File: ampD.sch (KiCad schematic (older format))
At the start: 9 parts, among them U3 MCP6004, U4 Mux

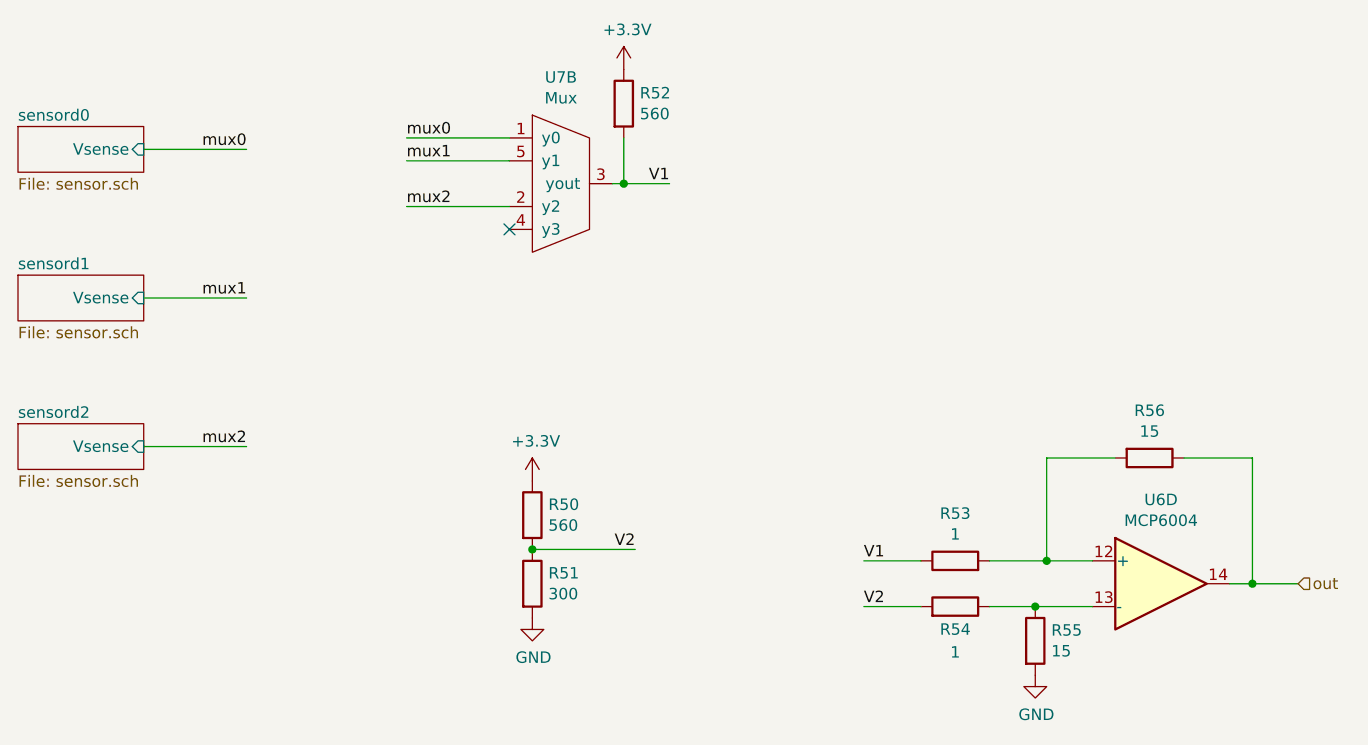
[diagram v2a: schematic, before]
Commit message: fixed drc errors
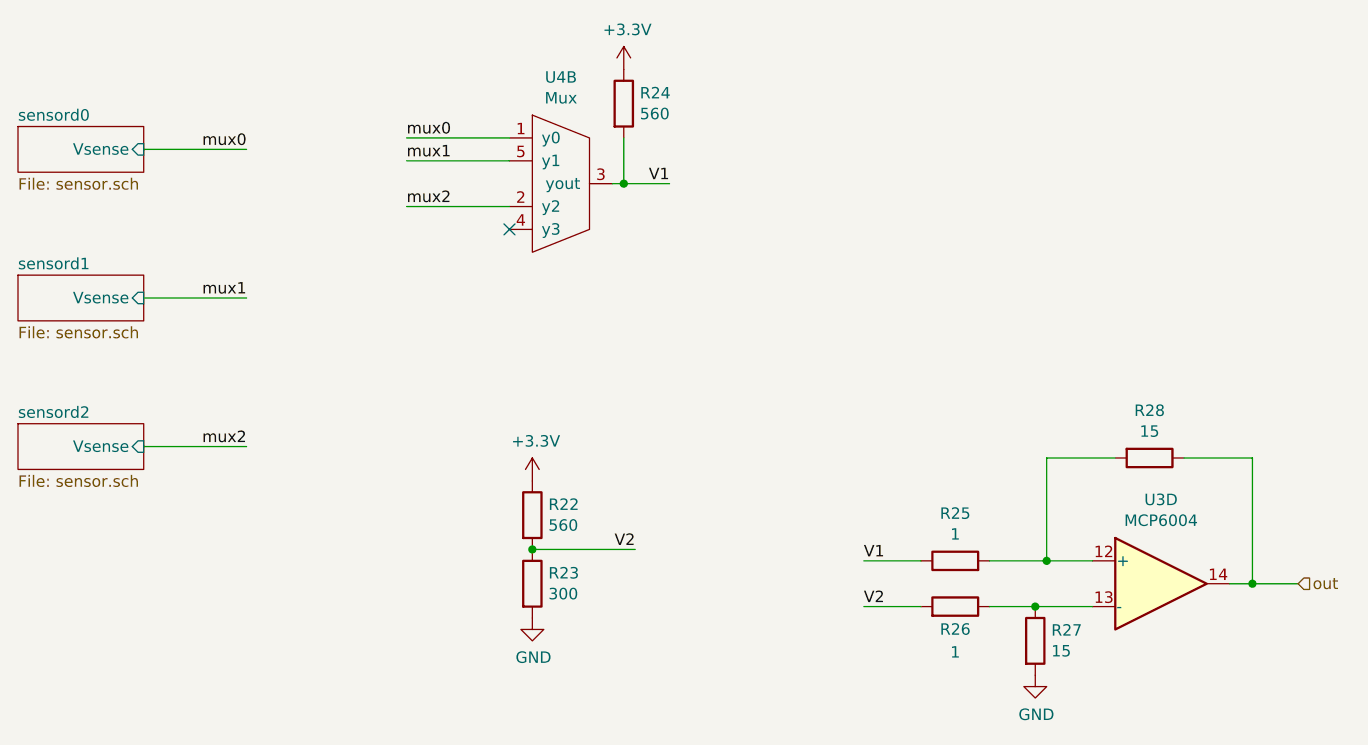
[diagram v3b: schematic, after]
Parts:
- U3: footprint Package_DIP:DIP-14_W7.62mm -> Package_SO:SOIC-16_3.9x9.9mm_P1.27mm
- U4: footprint Package_DIP:DIP-16_W7.62mm -> Package_SO:SOIC-16_3.9x9.9mm_P1.27mm
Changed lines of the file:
@@
 AR Path="/6019DBCE/6015EF5C" Ref="R27"  Part="1"
 AR Path="/601B4C19/6015EF5C" Ref="R55"  Part="1"
-F 0 "R55" H 5520 4096 50  0000 L CNN
+F 0 "R27" H 5520 4096 50  0000 L CNN
 F 1 "15" H 5520 4005 50  0000 L CNN
 F 2 "Resistor_THT:R_Axial_DIN0204_L3.6mm_D1.6mm_P5.08mm_Horizontal" V 5380 4050 50  0001 C CNN
@@
 AR Path="/6019DBCE/6019E3A7" Ref="R28"  Part="1"
 AR Path="/601B4C19/6019E3A7" Ref="R56"  Part="1"
-F 0 "R56" V 5743 3250 50  0000 C CNN
+F 0 "R28" V 5743 3250 50  0000 C CNN
 F 1 "15" V 5834 3250 50  0000 C CNN
 F 2 "Resistor_THT:R_Axial_DIN0204_L3.6mm_D1.6mm_P5.08mm_Horizontal" V 5880 3250 50  0001 C CNN
@@
 AR Path="/6019DBCE/6019E3B2" Ref="R25"  Part="1"
 AR Path="/601B4C19/6019E3B2" Ref="R53"  Part="1"
-F 0 "R53" V 5307 3700 50  0000 C CNN
+F 0 "R25" V 5307 3700 50  0000 C CNN
 F 1 "1" V 5216 3700 50  0000 C CNN
 F 2 "Resistor_THT:R_Axial_DIN0204_L3.6mm_D1.6mm_P5.08mm_Horizontal" V 5030 3700 50  0001 C CNN
@@
 AR Path="/6019DBCE/6019E3A8" Ref="R26"  Part="1"
 AR Path="/601B4C19/6019E3A8" Ref="R54"  Part="1"
-F 0 "R54" V 5000 3900 50  0000 C CNN
+F 0 "R26" V 5000 3900 50  0000 C CNN
 F 1 "1" V 4900 3900 50  0000 C CNN
 F 2 "Resistor_THT:R_Axial_DIN0204_L3.6mm_D1.6mm_P5.08mm_Horizontal" V 5030 3900 50  0001 C CNN
@@
 AR Path="/6019DBCE/6019E3B3" Ref="R22"  Part="1"
 AR Path="/601B4C19/6019E3B3" Ref="R50"  Part="1"
-F 0 "R50" H 3320 3546 50  0000 L CNN
+F 0 "R22" H 3320 3546 50  0000 L CNN
 F 1 "560" H 3320 3455 50  0000 L CNN
 F 2 "Resistor_THT:R_Axial_DIN0204_L3.6mm_D1.6mm_P5.08mm_Horizontal" V 3180 3500 50  0001 C CNN
@@
 AR Path="/6019DBCE/60198F36" Ref="R23"  Part="1"
 AR Path="/601B4C19/60198F36" Ref="R51"  Part="1"
-F 0 "R51" H 3320 3846 50  0000 L CNN
+F 0 "R23" H 3320 3846 50  0000 L CNN
 F 1 "300" H 3320 3755 50  0000 L CNN
 F 2 "Resistor_THT:R_Axial_DIN0204_L3.6mm_D1.6mm_P5.08mm_Horizontal" V 3180 3800 50  0001 C CNN
@@
 AR Path="/6019DBCE/6017A5CD" Ref="U4"  Part="2"
 AR Path="/601B4C19/6017A5CD" Ref="U7"  Part="2"
-F 0 "U7" H 3375 2515 50  0000 C CNN
+F 0 "U4" H 3375 2515 50  0000 C CNN
 F 1 "Mux" H 3375 2424 50  0000 C CNN
-F 2 "Package_DIP:DIP-16_W7.62mm" H 3350 2050 50  0001 C CNN
+F 2 "Package_SO:SOIC-16_3.9x9.9mm_P1.27mm" H 3350 2050 50  0001 C CNN
 F 3 "" H 3350 2050 50  0001 C CNN
 	2    3350 2050
@@
 AR Path="/6019DBCE/6018F24E" Ref="U3"  Part="4"
 AR Path="/601B4C19/6018F24E" Ref="U6"  Part="4"
-F 0 "U6" H 6000 4167 50  0000 C CNN
+F 0 "U3" H 6000 4167 50  0000 C CNN
 F 1 "MCP6004" H 6000 4076 50  0000 C CNN
-F 2 "Package_DIP:DIP-14_W7.62mm" H 5950 3900 50  0001 C CNN
+F 2 "Package_SO:SOIC-16_3.9x9.9mm_P1.27mm" H 5950 3900 50  0001 C CNN
 F 3 "http://ww1.microchip.com/downloads/en/DeviceDoc/21733j.pdf" H 6050 4000 50  0001 C CNN
 	4    6000 3800
@@
 AR Path="/6019DBCE/60204E98" Ref="R24"  Part="1"
 AR Path="/601B4C19/60204E98" Ref="R52"  Part="1"
-F 0 "R52" H 3720 1746 50  0000 L CNN
+F 0 "R24" H 3720 1746 50  0000 L CNN
 F 1 "560" H 3720 1655 50  0000 L CNN
 F 2 "Resistor_THT:R_Axial_DIN0204_L3.6mm_D1.6mm_P5.08mm_Horizontal" V 3580 1700 50  0001 C CNN

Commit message: switched over remaining rs to 0805
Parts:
- R22, R23, R24, R25, R26, R27, R28: footprint Resistor_THT:R_Axial_DIN0204_L3.6mm_D1.6mm_P5.08mm_Horizontal -> Resistor_SMD:R_0805_2012Metric_Pad1.20x1.40mm_HandSolder
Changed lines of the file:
@@
 F 0 "R27" H 5520 4096 50  0000 L CNN
 F 1 "15" H 5520 4005 50  0000 L CNN
-F 2 "Resistor_THT:R_Axial_DIN0204_L3.6mm_D1.6mm_P5.08mm_Horizontal" V 5380 4050 50  0001 C CNN
+F 2 "Resistor_SMD:R_0805_2012Metric_Pad1.20x1.40mm_HandSolder" V 5380 4050 50  0001 C CNN
 F 3 "~" H 5450 4050 50  0001 C CNN
 	1    5450 4050
@@
 F 0 "R28" V 5743 3250 50  0000 C CNN
 F 1 "15" V 5834 3250 50  0000 C CNN
-F 2 "Resistor_THT:R_Axial_DIN0204_L3.6mm_D1.6mm_P5.08mm_Horizontal" V 5880 3250 50  0001 C CNN
+F 2 "Resistor_SMD:R_0805_2012Metric_Pad1.20x1.40mm_HandSolder" V 5880 3250 50  0001 C CNN
 F 3 "~" H 5950 3250 50  0001 C CNN
 	1    5950 3250
@@
 F 0 "R25" V 5307 3700 50  0000 C CNN
 F 1 "1" V 5216 3700 50  0000 C CNN
-F 2 "Resistor_THT:R_Axial_DIN0204_L3.6mm_D1.6mm_P5.08mm_Horizontal" V 5030 3700 50  0001 C CNN
+F 2 "Resistor_SMD:R_0805_2012Metric_Pad1.20x1.40mm_HandSolder" V 5030 3700 50  0001 C CNN
 F 3 "~" H 5100 3700 50  0001 C CNN
 	1    5100 3700
@@
 F 0 "R26" V 5000 3900 50  0000 C CNN
 F 1 "1" V 4900 3900 50  0000 C CNN
-F 2 "Resistor_THT:R_Axial_DIN0204_L3.6mm_D1.6mm_P5.08mm_Horizontal" V 5030 3900 50  0001 C CNN
+F 2 "Resistor_SMD:R_0805_2012Metric_Pad1.20x1.40mm_HandSolder" V 5030 3900 50  0001 C CNN
 F 3 "~" H 5100 3900 50  0001 C CNN
 	1    5100 3900
@@
 F 0 "R22" H 3320 3546 50  0000 L CNN
 F 1 "560" H 3320 3455 50  0000 L CNN
-F 2 "Resistor_THT:R_Axial_DIN0204_L3.6mm_D1.6mm_P5.08mm_Horizontal" V 3180 3500 50  0001 C CNN
+F 2 "Resistor_SMD:R_0805_2012Metric_Pad1.20x1.40mm_HandSolder" V 3180 3500 50  0001 C CNN
 F 3 "~" H 3250 3500 50  0001 C CNN
 	1    3250 3500
@@
 F 0 "R23" H 3320 3846 50  0000 L CNN
 F 1 "300" H 3320 3755 50  0000 L CNN
-F 2 "Resistor_THT:R_Axial_DIN0204_L3.6mm_D1.6mm_P5.08mm_Horizontal" V 3180 3800 50  0001 C CNN
+F 2 "Resistor_SMD:R_0805_2012Metric_Pad1.20x1.40mm_HandSolder" V 3180 3800 50  0001 C CNN
 F 3 "~" H 3250 3800 50  0001 C CNN
 	1    3250 3800
@@
 F 0 "R24" H 3720 1746 50  0000 L CNN
 F 1 "560" H 3720 1655 50  0000 L CNN
-F 2 "Resistor_THT:R_Axial_DIN0204_L3.6mm_D1.6mm_P5.08mm_Horizontal" V 3580 1700 50  0001 C CNN
+F 2 "Resistor_SMD:R_0805_2012Metric_Pad1.20x1.40mm_HandSolder" V 3580 1700 50  0001 C CNN
 F 3 "~" H 3650 1700 50  0001 C CNN
 	1    3650 1700

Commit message: fixed issue with wrong amp footprint
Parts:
- U3: footprint Package_SO:SOIC-16_3.9x9.9mm_P1.27mm -> Package_SO:SOIC-14_3.9x8.7mm_P1.27mm
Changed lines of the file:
@@
 F 0 "U3" H 6000 4167 50  0000 C CNN
 F 1 "MCP6004" H 6000 4076 50  0000 C CNN
-F 2 "Package_SO:SOIC-16_3.9x9.9mm_P1.27mm" H 5950 3900 50  0001 C CNN
+F 2 "Package_SO:SOIC-14_3.9x8.7mm_P1.27mm" H 5950 3900 50  0001 C CNN
 F 3 "http://ww1.microchip.com/downloads/en/DeviceDoc/21733j.pdf" H 6050 4000 50  0001 C CNN
 	4    6000 3800

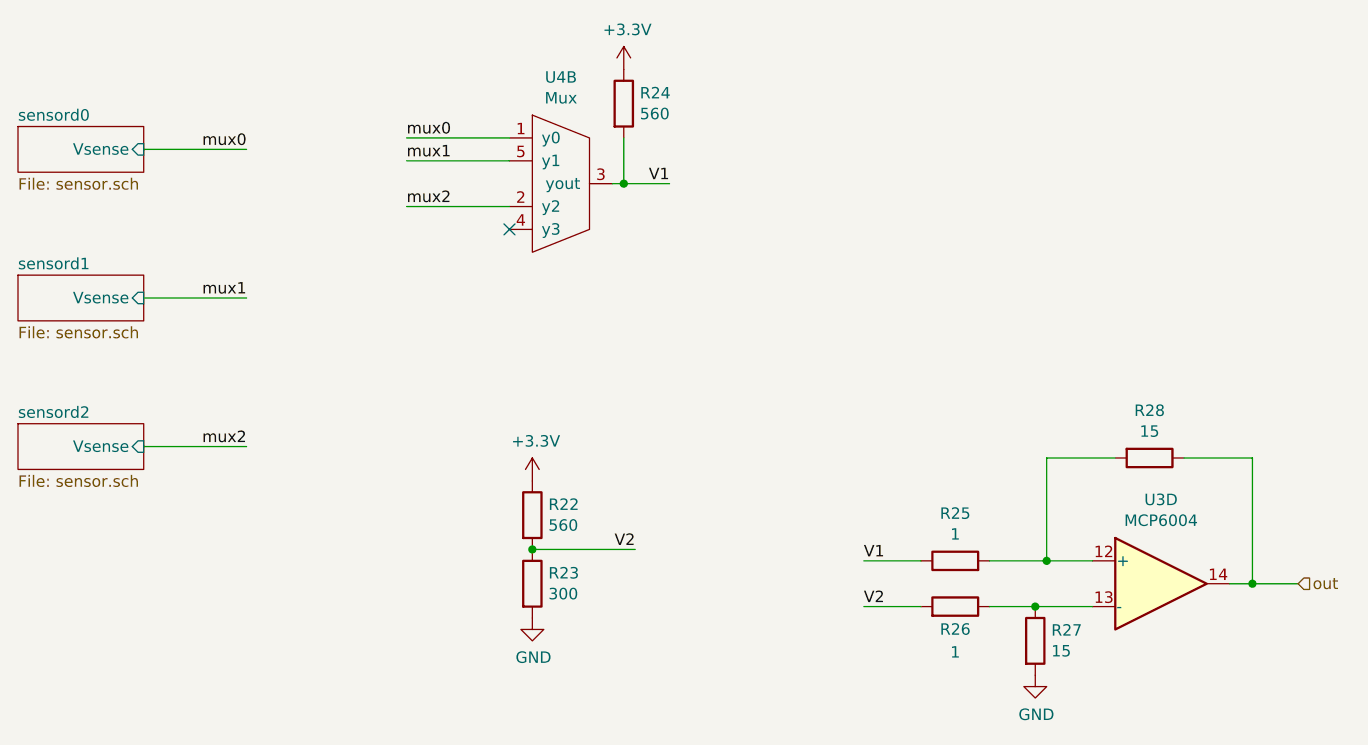
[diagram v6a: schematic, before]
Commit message: reverted back to screw terminals
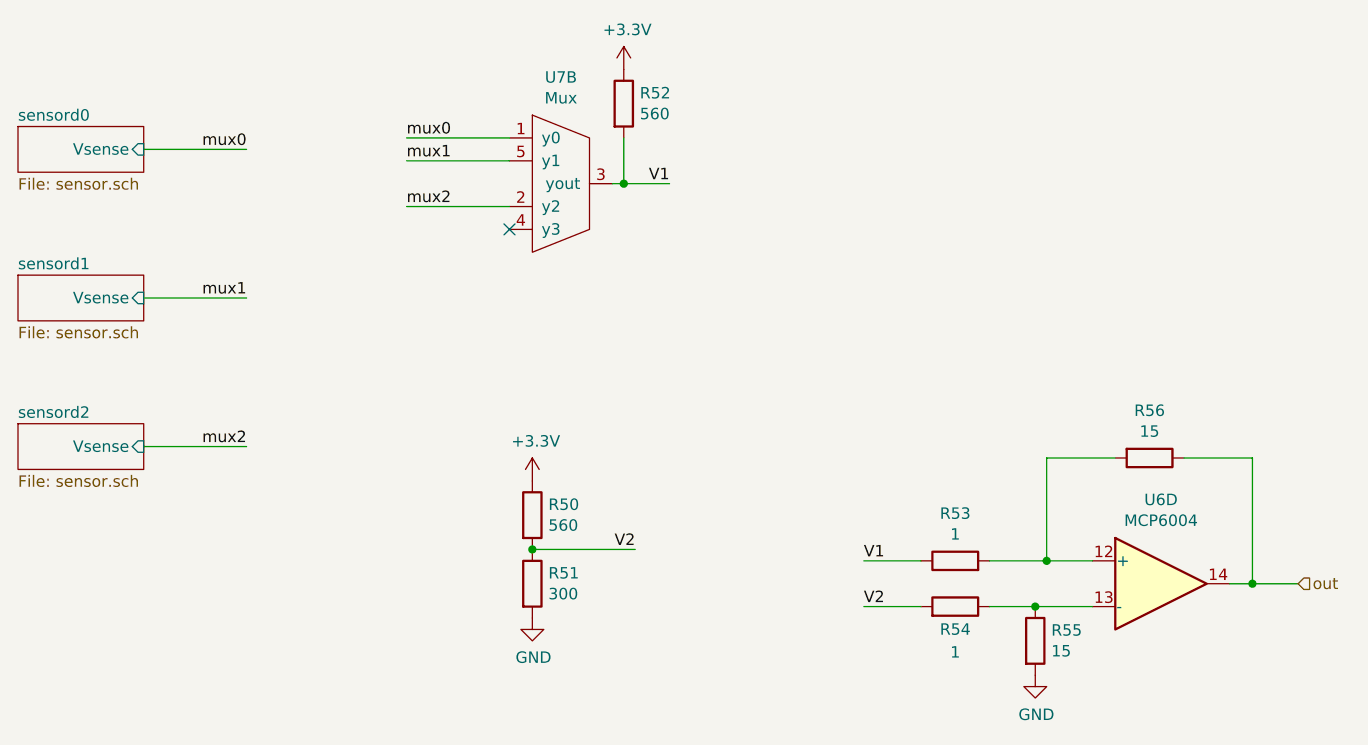
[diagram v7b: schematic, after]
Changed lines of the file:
@@
 AR Path="/6019DBCE/6015EF5C" Ref="R27"  Part="1"
 AR Path="/601B4C19/6015EF5C" Ref="R55"  Part="1"
-F 0 "R27" H 5520 4096 50  0000 L CNN
+F 0 "R55" H 5520 4096 50  0000 L CNN
 F 1 "15" H 5520 4005 50  0000 L CNN
 F 2 "Resistor_SMD:R_0805_2012Metric_Pad1.20x1.40mm_HandSolder" V 5380 4050 50  0001 C CNN
@@
 AR Path="/6019DBCE/6019E3A7" Ref="R28"  Part="1"
 AR Path="/601B4C19/6019E3A7" Ref="R56"  Part="1"
-F 0 "R28" V 5743 3250 50  0000 C CNN
+F 0 "R56" V 5743 3250 50  0000 C CNN
 F 1 "15" V 5834 3250 50  0000 C CNN
 F 2 "Resistor_SMD:R_0805_2012Metric_Pad1.20x1.40mm_HandSolder" V 5880 3250 50  0001 C CNN
@@
 AR Path="/6019DBCE/6019E3B2" Ref="R25"  Part="1"
 AR Path="/601B4C19/6019E3B2" Ref="R53"  Part="1"
-F 0 "R25" V 5307 3700 50  0000 C CNN
+F 0 "R53" V 5307 3700 50  0000 C CNN
 F 1 "1" V 5216 3700 50  0000 C CNN
 F 2 "Resistor_SMD:R_0805_2012Metric_Pad1.20x1.40mm_HandSolder" V 5030 3700 50  0001 C CNN
@@
 AR Path="/6019DBCE/6019E3A8" Ref="R26"  Part="1"
 AR Path="/601B4C19/6019E3A8" Ref="R54"  Part="1"
-F 0 "R26" V 5000 3900 50  0000 C CNN
+F 0 "R54" V 5000 3900 50  0000 C CNN
 F 1 "1" V 4900 3900 50  0000 C CNN
 F 2 "Resistor_SMD:R_0805_2012Metric_Pad1.20x1.40mm_HandSolder" V 5030 3900 50  0001 C CNN
@@
 AR Path="/6019DBCE/6019E3B3" Ref="R22"  Part="1"
 AR Path="/601B4C19/6019E3B3" Ref="R50"  Part="1"
-F 0 "R22" H 3320 3546 50  0000 L CNN
+F 0 "R50" H 3320 3546 50  0000 L CNN
 F 1 "560" H 3320 3455 50  0000 L CNN
 F 2 "Resistor_SMD:R_0805_2012Metric_Pad1.20x1.40mm_HandSolder" V 3180 3500 50  0001 C CNN
@@
 AR Path="/6019DBCE/60198F36" Ref="R23"  Part="1"
 AR Path="/601B4C19/60198F36" Ref="R51"  Part="1"
-F 0 "R23" H 3320 3846 50  0000 L CNN
+F 0 "R51" H 3320 3846 50  0000 L CNN
 F 1 "300" H 3320 3755 50  0000 L CNN
 F 2 "Resistor_SMD:R_0805_2012Metric_Pad1.20x1.40mm_HandSolder" V 3180 3800 50  0001 C CNN
@@
 AR Path="/6019DBCE/60198F37" Ref="#PWR035"  Part="1"
 AR Path="/601B4C19/60198F37" Ref="#PWR069"  Part="1"
-F 0 "#PWR035" H 3250 3200 50  0001 C CNN
+F 0 "#PWR069" H 3250 3200 50  0001 C CNN
 F 1 "+3.3V" H 3265 3523 50  0000 C CNN
 F 2 "" H 3250 3350 50  0001 C CNN
@@
 AR Path="/6019DBCE/6019E3A9" Ref="#PWR036"  Part="1"
 AR Path="/601B4C19/6019E3A9" Ref="#PWR070"  Part="1"
-F 0 "#PWR036" H 3250 3700 50  0001 C CNN
+F 0 "#PWR070" H 3250 3700 50  0001 C CNN
 F 1 "GND" H 3255 3777 50  0000 C CNN
 F 2 "" H 3250 3950 50  0001 C CNN
@@
 AR Path="/6019DBCE/60198F29" Ref="#PWR038"  Part="1"
 AR Path="/601B4C19/60198F29" Ref="#PWR072"  Part="1"
-F 0 "#PWR038" H 5450 3950 50  0001 C CNN
+F 0 "#PWR072" H 5450 3950 50  0001 C CNN
 F 1 "GND" H 5455 4027 50  0000 C CNN
 F 2 "" H 5450 4200 50  0001 C CNN
@@
 AR Path="/6019DBCE/6017A5CD" Ref="U4"  Part="2"
 AR Path="/601B4C19/6017A5CD" Ref="U7"  Part="2"
-F 0 "U4" H 3375 2515 50  0000 C CNN
+F 0 "U7" H 3375 2515 50  0000 C CNN
 F 1 "Mux" H 3375 2424 50  0000 C CNN
 F 2 "Package_SO:SOIC-16_3.9x9.9mm_P1.27mm" H 3350 2050 50  0001 C CNN
@@
 AR Path="/6019DBCE/6018F24E" Ref="U3"  Part="4"
 AR Path="/601B4C19/6018F24E" Ref="U6"  Part="4"
-F 0 "U3" H 6000 4167 50  0000 C CNN
+F 0 "U6" H 6000 4167 50  0000 C CNN
 F 1 "MCP6004" H 6000 4076 50  0000 C CNN
 F 2 "Package_SO:SOIC-14_3.9x8.7mm_P1.27mm" H 5950 3900 50  0001 C CNN
@@
 AR Path="/6019DBCE/60204FC0" Ref="#PWR037"  Part="1"
 AR Path="/601B4C19/60204FC0" Ref="#PWR071"  Part="1"
-F 0 "#PWR037" H 3650 1400 50  0001 C CNN
+F 0 "#PWR071" H 3650 1400 50  0001 C CNN
 F 1 "+3.3V" H 3665 1723 50  0000 C CNN
 F 2 "" H 3650 1550 50  0001 C CNN
@@
 AR Path="/6019DBCE/60204E98" Ref="R24"  Part="1"
 AR Path="/601B4C19/60204E98" Ref="R52"  Part="1"
-F 0 "R24" H 3720 1746 50  0000 L CNN
+F 0 "R52" H 3720 1746 50  0000 L CNN
 F 1 "560" H 3720 1655 50  0000 L CNN
 F 2 "Resistor_SMD:R_0805_2012Metric_Pad1.20x1.40mm_HandSolder" V 3580 1700 50  0001 C CNN

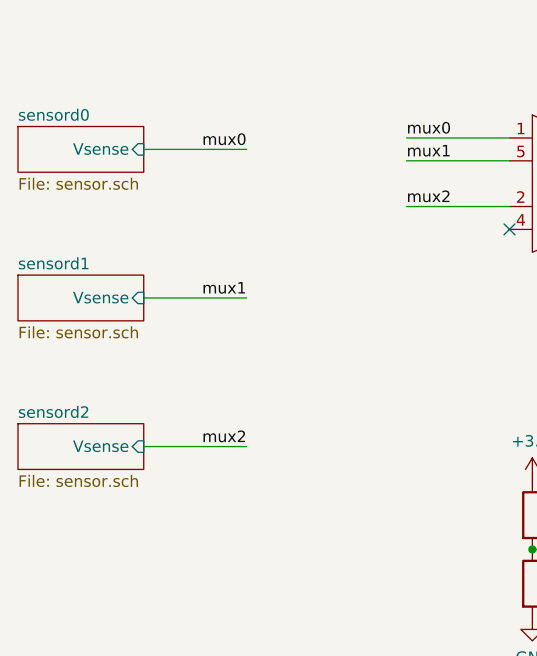
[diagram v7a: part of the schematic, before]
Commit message: updated sch with pico connectors
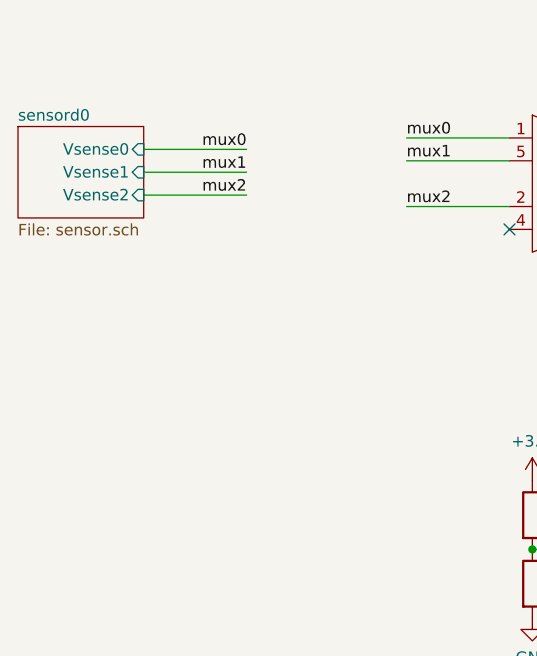
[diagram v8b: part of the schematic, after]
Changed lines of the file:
@@
 $Descr A4 11693 8268
 encoding utf-8
-Sheet 14 41
+Sheet 16 21
 Title ""
 Date ""
@@
 mux0
 $Sheet
-S 1000 1800 550  200
+S 1000 1800 550  400
 U 601A6FCC
 F0 "sensord0" 50
 F1 "sensor.sch" 50
-F2 "Vsense" I R 1550 1900 50
+F2 "Vsense0" I R 1550 1900 50
+F3 "Vsense1" I R 1550 2000 50
+F4 "Vsense2" I R 1550 2100 50
 $EndSheet
-Wire Wire Line
-	1550 2550 2000 2550
-Text Label 2000 2550 2    50   ~ 0
+Text Label 2000 2000 2    50   ~ 0
 mux1
-$Sheet
-S 1000 2450 550  200
-U 601A6FD1
-F0 "sensord1" 50
-F1 "sensor.sch" 50
-F2 "Vsense" I R 1550 2550 50
-$EndSheet
-Wire Wire Line
-	1550 3200 2000 3200
-Text Label 2000 3200 2    50   ~ 0
+Text Label 2000 2100 2    50   ~ 0
 mux2
-$Sheet
-S 1000 3100 550  200
-U 601A6FD6
-F0 "sensord2" 50
-F1 "sensor.sch" 50
-F2 "Vsense" I R 1550 3200 50
-$EndSheet
 $Comp
 L power:+3.3V #PWR?
@@
 	1    0    0    -1
 $EndComp
+Wire Wire Line
+	2000 2000 1550 2000
+Wire Wire Line
+	1550 2100 2000 2100
 $EndSCHEMATC
